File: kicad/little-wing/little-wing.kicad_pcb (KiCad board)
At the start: 4 copper layers, 16.1 x 57.1 mm, 63 parts, among them J1 Battery pack, J1 HRO_TYPE-C-31-M-14, J2 Battery, J3 rgb, J4 columns, J5 Conn_01x10, J6 rows, J7 sensor, Q1 AO3401A, Q2 2N7002, SW1 Battery, SW2 Reset, U1 nPM1100-CAAx, U1 nRF52840_CKAA, X1 32MHz, X2 32.768kHz

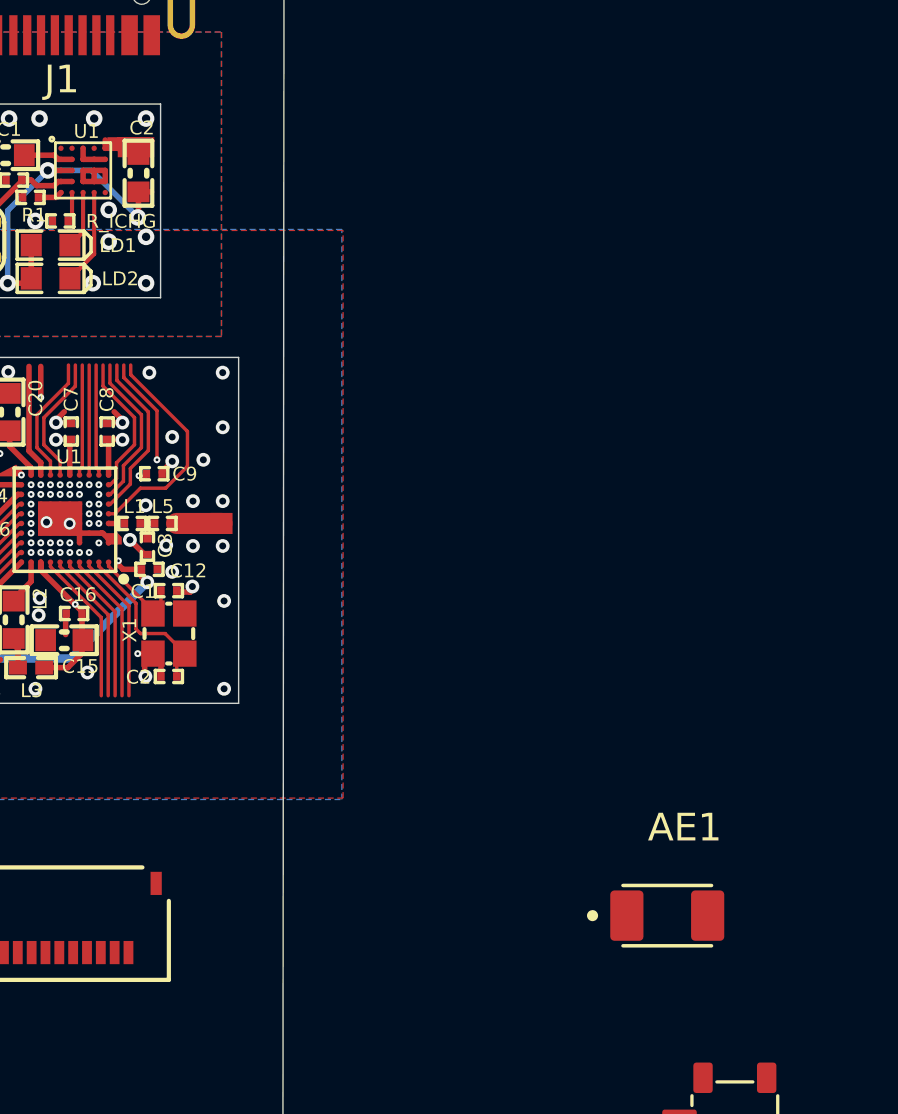
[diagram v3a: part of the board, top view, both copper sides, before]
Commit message: Adding the antennae
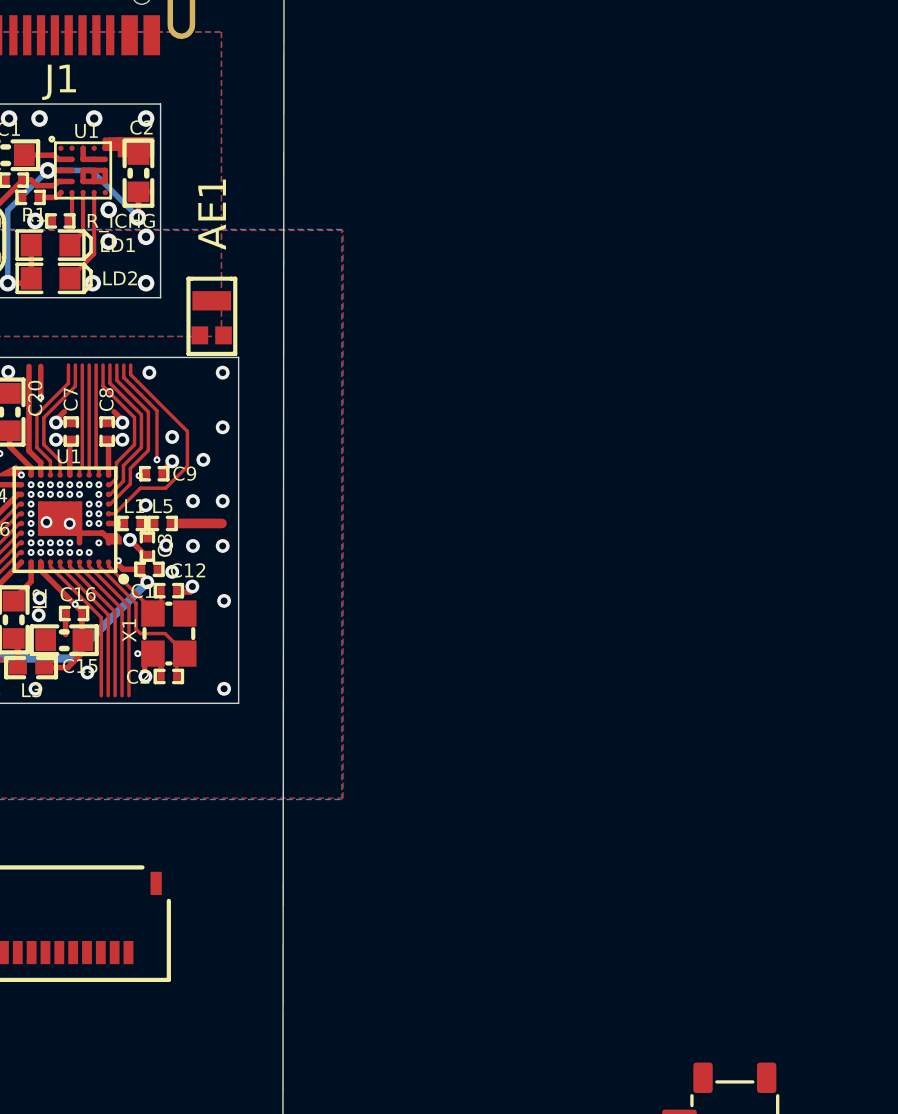
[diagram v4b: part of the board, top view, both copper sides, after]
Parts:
- AE1: footprint JTI Antenna:ANTC3216X140N -> YAGEO Antenna:ANT2012LL13R2400A
- moved AE1 27.1 mm to (155.5, 74.4), turned to 90 degrees
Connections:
- AE1 pad 1: /Main Module/MCU/RF -> RF
- AE1 pad 2: (no net) -> GND
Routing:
- net RF: vias 0 -> 2
- net GND: vias 57 -> 55

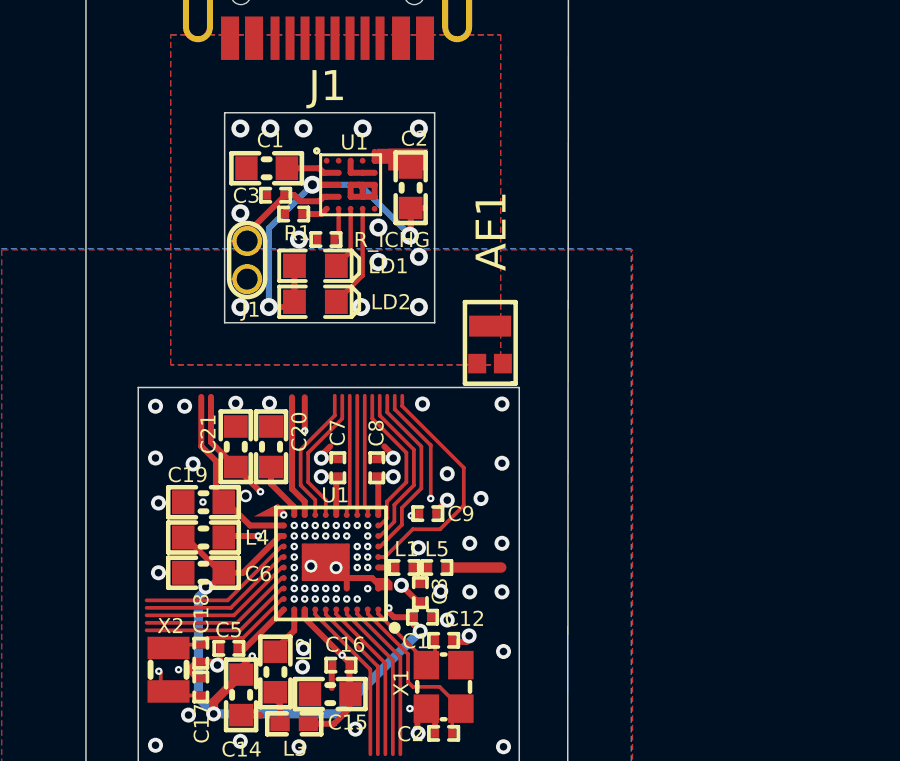
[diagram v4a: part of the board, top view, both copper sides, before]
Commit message: Removing the NFC1/2 connectors
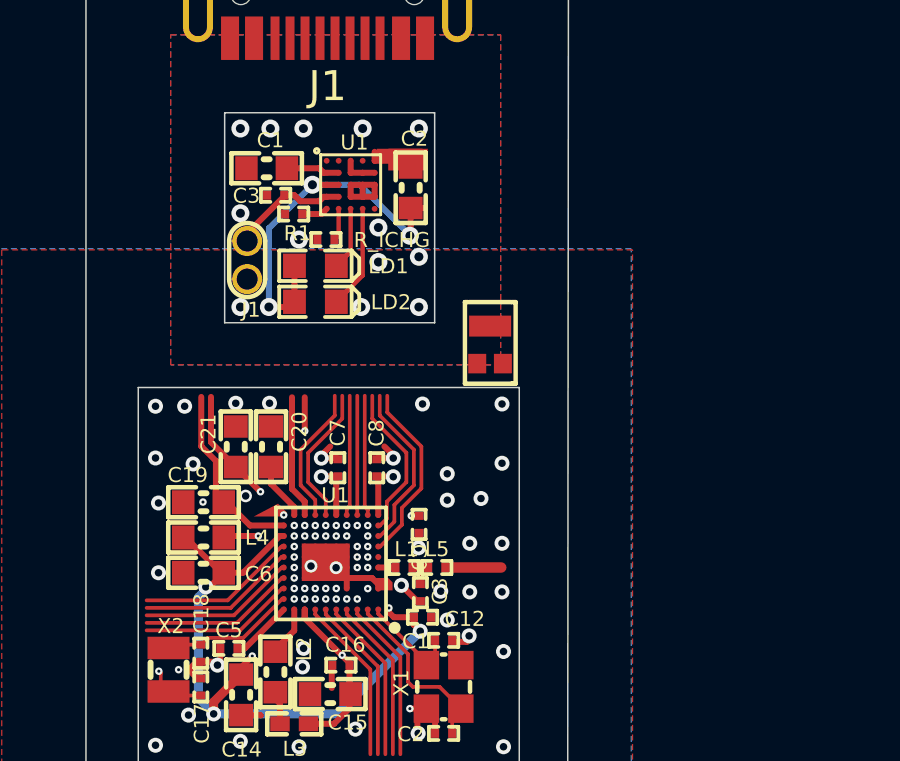
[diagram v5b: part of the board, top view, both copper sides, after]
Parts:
- moved C9 0.46 mm to (153.1, 80.4), turned to -90 degrees
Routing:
- net P0.09/NFC1: track 8.07 -> 0.00 mm
- net P0.10/NFC2: track 7.25 -> 0.00 mm, vias 2 -> 1

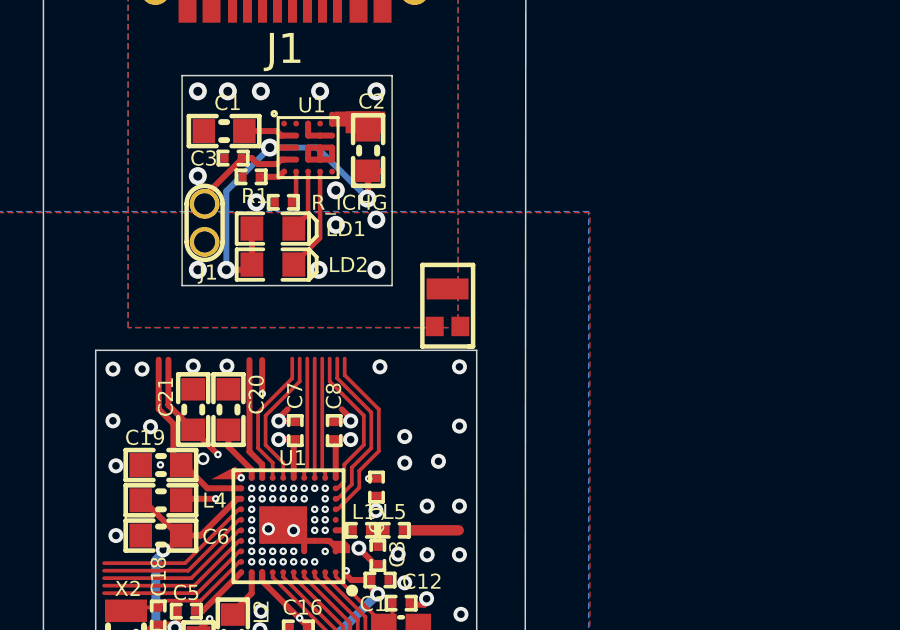
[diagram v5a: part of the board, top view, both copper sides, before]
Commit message: Cleaning up the PSU schematics
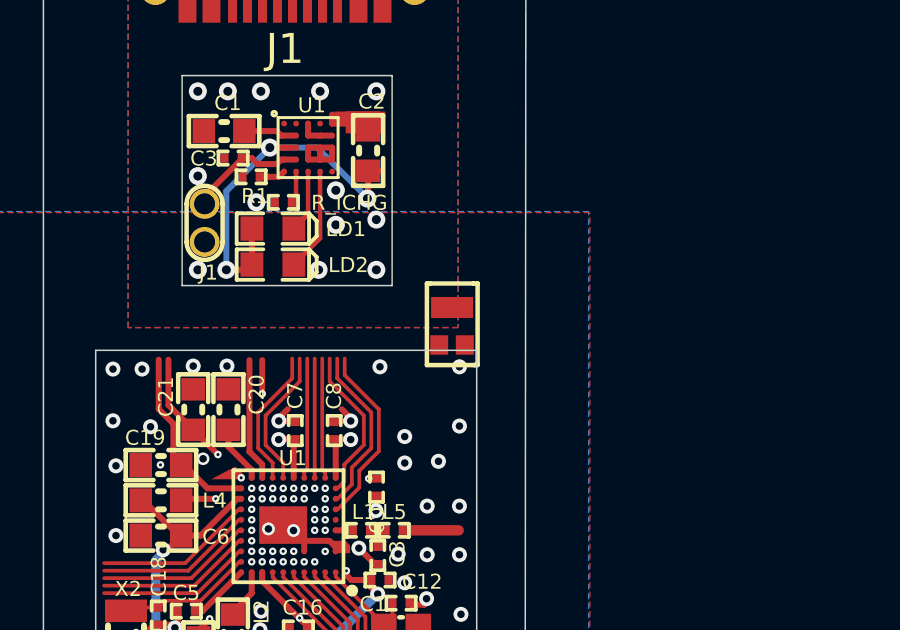
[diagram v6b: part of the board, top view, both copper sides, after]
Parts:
- moved AE1 0.64 mm to (155.6, 75.0)

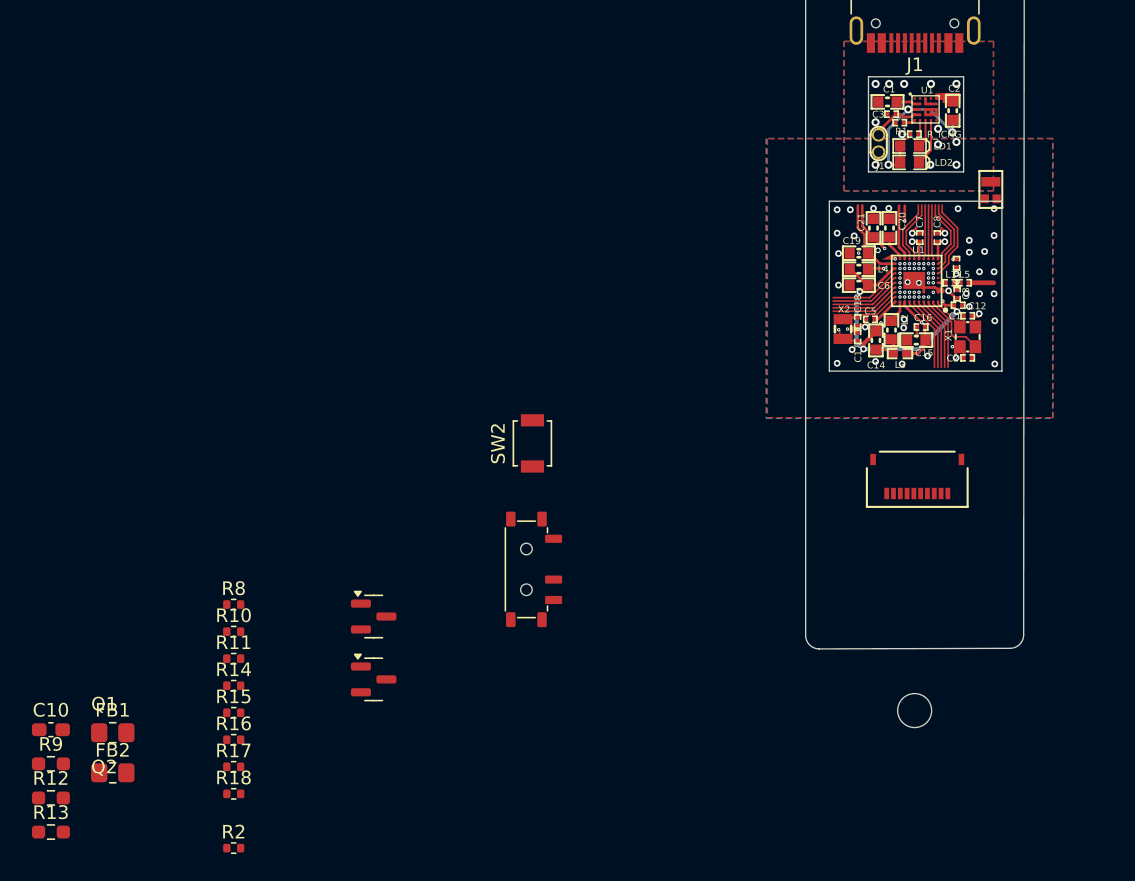
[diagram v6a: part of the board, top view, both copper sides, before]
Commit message: Updating schematics/pcb to match the labels
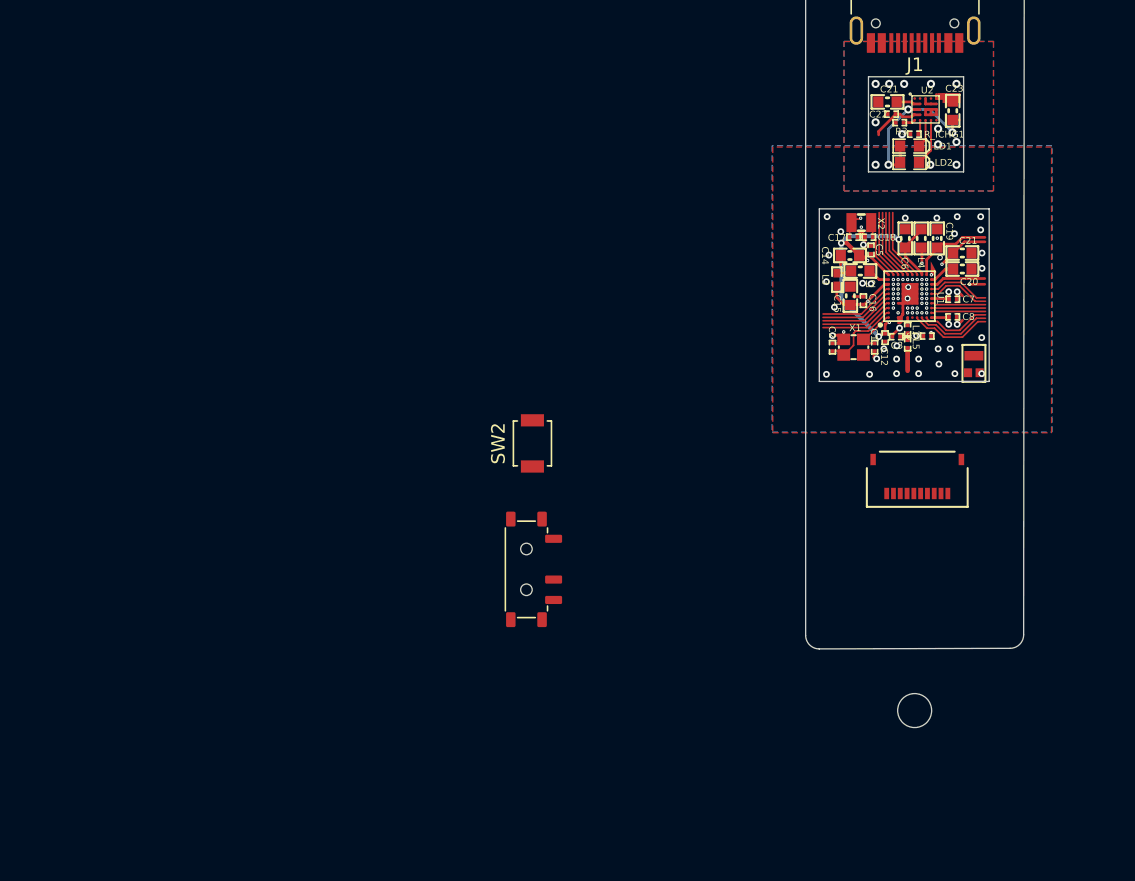
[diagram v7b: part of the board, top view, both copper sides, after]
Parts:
- removed C10: 1uF, Capacitor_SMD:C_0603_1608Metric_Pad1.08x0.95mm_HandSolder
- removed FB1, FB2: 2.7k, Resistor_SMD:R_0805_2012Metric_Pad1.20x1.40mm_HandSolder
- removed the J1 at (147.3, 71.6)
- removed Q1: AO3401A, Package_TO_SOT_SMD:SOT-23
- removed Q2: 2N7002, Package_TO_SOT_SMD:SOT-23
- removed R10, R18: 10k, Resistor_SMD:R_0402_1005Metric
- removed R11, R14, R15, R16, R17, R8: 100R, Resistor_SMD:R_0402_1005Metric
- removed R12, R13, R9: 10k, Resistor_SMD:R_0603_1608Metric_Pad0.98x0.95mm_HandSolder
- removed R2: 5k1, Resistor_SMD:R_0402_1005Metric
- moved AE1 12.9 mm to (154.4, 87.8)
- moved C2 9.98 mm to (143.9, 86.6), turned to 90 degrees
- moved X1 8.43 mm to (145.5, 86.6), turned to 180 degrees
- moved X2 7.95 mm to (146.1, 77.4), turned to 0 degrees
- moved C17 7.34 mm to (145.5, 78.5), turned to 0 degrees
- moved C1 7.23 mm to (147.0, 86.6), turned to -90 degrees
- moved L3 7.16 mm to (144.3, 81.6), turned to 90 degrees
- moved C21 6.79 mm to (153.5, 79.7), turned to 0 degrees
- moved C14 6.54 mm to (145.2, 79.8), turned to 180 degrees
- moved C18 6.26 mm to (146.6, 78.5), turned to 180 degrees
- moved L5 6.16 mm to (149.5, 86.4), turned to -90 degrees
- moved C20 6.15 mm to (153.5, 80.8), turned to 0 degrees
- moved C8 5.95 mm to (152.8, 84.4), turned to 0 degrees
- moved C12 5.87 mm to (147.8, 85.9), turned to -90 degrees
- moved C19 5.86 mm to (151.6, 78.6), turned to 90 degrees
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- renumbered C1 to C21, C3 to C22, C2 to C23, R1 to R3, R_ICHG to R_ICHG1, U1 to U2
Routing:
- net GND: vias 55 -> 54
- net RF: vias 2 -> 3
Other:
- outline, holes or cut-outs redrawn
